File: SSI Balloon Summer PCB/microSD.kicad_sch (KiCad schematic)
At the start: 5 parts, among them J6 1040310811

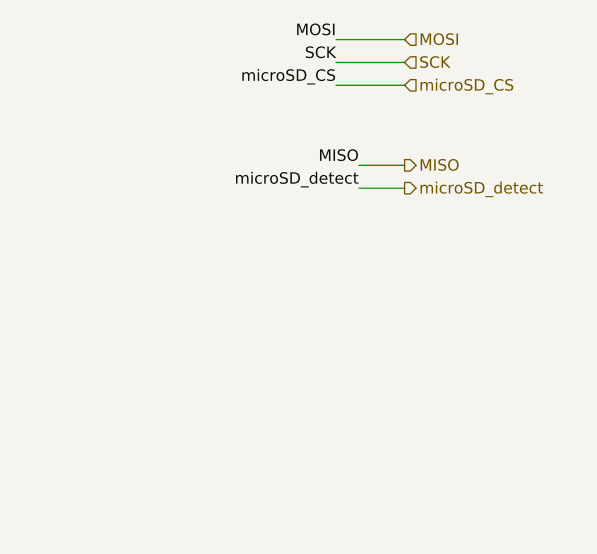
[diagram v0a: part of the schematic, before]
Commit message: Finished sensors + tidied up schematic
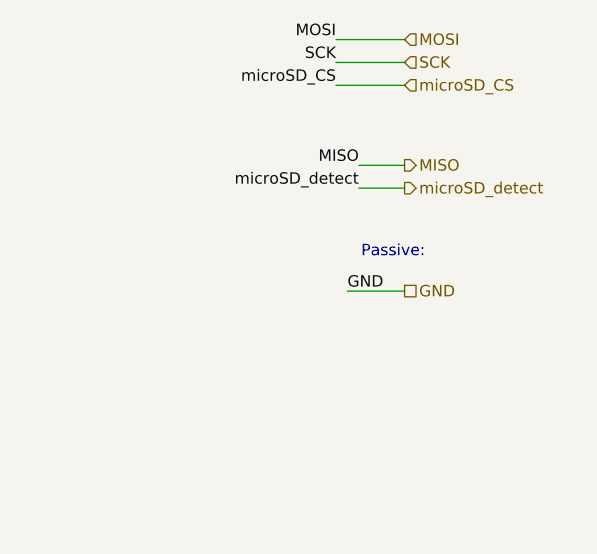
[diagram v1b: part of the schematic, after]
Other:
- note added: "Passive:"
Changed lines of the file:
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@@
 	(generator_version "10.0")
 	(paper "A4")
+	(text "Passive:"
+		(exclude_from_sim no)
+		(at 246.38 52.832 0)
+		(effects
+			(font
+				(size 1.27 1.27)
+			)
+		)
+	)
 	(text "microSD_detect: \nhigh if SD card detected\nlow if no SD card"
 		(exclude_from_sim no)
@@
 	(wire
 		(pts
+			(xy 241.3 57.15) (xy 247.65 57.15)
+		)
+		(stroke
+			(width 0)
+			(type default)
+		)
+	)
+	(wire
+		(pts
 			(xy 66.04 78.74) (xy 69.85 78.74)
 		)
@@
 		)
 	)
+	(label "GND"
+		(at 241.3 57.15 0)
+		(effects
+			(font
+				(size 1.27 1.27)
+			)
+			(justify left bottom)
+		)
+	)
 	(label "microSD_detect"
 		(at 144.78 78.74 180)
@@
 		)
 	)
+	(hierarchical_label "GND"
+		(shape passive)
+		(at 247.65 57.15 0)
+		(effects
+			(font
+				(size 1.27 1.27)
+			)
+			(justify left)
+		)
+	)

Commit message: Fixed I2C and SPI issues
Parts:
- added R26: 10k, symbol Device:R
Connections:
- net +3V3: now also R26.2
- net microSD_CS: now also R26.1
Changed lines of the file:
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@@
+	)
+	(junction
+		(at 62.23 78.74)
+		(diameter 0)
+		(color 0 0 0 0)
 	)
 	(junction
@@
 	(wire
 		(pts
+			(xy 62.23 76.2) (xy 62.23 78.74)
+		)
+		(stroke
+			(width 0)
+			(type default)
+		)
+	)
+	(wire
+		(pts
 			(xy 241.3 57.15) (xy 247.65 57.15)
 		)
@@
 	(wire
 		(pts
-			(xy 66.04 78.74) (xy 69.85 78.74)
+			(xy 57.15 78.74) (xy 62.23 78.74)
+		)
+		(stroke
+			(width 0)
+			(type default)
+		)
+	)
+	(wire
+		(pts
+			(xy 62.23 66.04) (xy 62.23 68.58)
 		)
 		(stroke
@@
 		(pts
 			(xy 240.03 29.21) (xy 247.65 29.21)
+		)
+		(stroke
+			(width 0)
+			(type default)
+		)
+	)
+	(wire
+		(pts
+			(xy 62.23 78.74) (xy 69.85 78.74)
 		)
 		(stroke
@@
 	)
 	(label "microSD_CS"
-		(at 66.04 78.74 180)
+		(at 57.15 78.74 180)
 		(effects
 			(font
@@
 			)
 			(justify right bottom)
+		)
+	)
+	(label "+3V3"
+		(at 62.23 66.04 0)
+		(effects
+			(font
+				(size 1.27 1.27)
+			)
+			(justify left bottom)
 		)
 	)
@@
 					(unit 1)
 				)
+			)
+		)
+	)
+	(symbol
+		(lib_id "Device:R")
+		(at 62.23 72.39 180)
+		(unit 1)
+		(body_style 1)
+		(exclude_from_sim no)
+		(in_bom yes)
+		(on_board yes)
+		(in_pos_files yes)
+		(dnp no)
+		(property "Reference" "R26"
+			(at 60.198 73.66 0)
+			(show_name no)
+			(do_not_autoplace no)
+			(effects
+				(font
+					(size 1.27 1.27)
+				)
+				(justify left)
+			)
+		)
+		(property "Value" "10k"
+			(at 60.198 71.12 0)
+			(show_name no)
+			(do_not_autoplace no)
+			(effects
+				(font
+					(size 1.27 1.27)
+				)
+				(justify left)
+			)
+		)
+		(property "Footprint" ""
+			(at 64.008 72.39 90)
+			(hide yes)
+			(show_name no)
+			(do_not_autoplace no)
+			(effects
+				(font
+					(size 1.27 1.27)
+				)
+			)
+		)
+		(property "Datasheet" ""
+			(at 62.23 72.39 0)
+			(hide yes)
+			(show_name no)
+			(do_not_autoplace no)
+			(effects
+				(font
+					(size 1.27 1.27)
+				)
+			)
+		)
+		(property "Description" "Resistor"
+			(at 62.23 72.39 0)
+			(hide yes)
+			(show_name no)
+			(do_not_autoplace no)
+			(effects
+				(font
+					(size 1.27 1.27)
+				)
+			)
+		)
+		(pin "1"
+		)
+		(pin "2"
+		)
+		(instances
+			(project "SSI Summer Balloons"
+				(path "/3c45a535-6e6b-4825-ad52-82c10cbe7866/0df234a1-8d04-4ff9-99d5-3634fc842029"
+					(reference "R26")
+					(unit 1)
+				)

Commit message: Fixed ERC - no ERC errors
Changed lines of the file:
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@@
+	(wire
+		(pts
+			(xy 41.91 81.28) (xy 41.91 83.82)
+		)
+		(stroke
+			(width 0)
+			(type default)
+		)
+	)
+	(wire
+		(pts
+			(xy 125.73 78.74) (xy 144.78 78.74)
+		)
+		(stroke
+			(width 0)
+			(type default)
+		)
+	)
+	(wire
+		(pts
+			(xy 66.04 86.36) (xy 69.85 86.36)
+		)
+		(stroke
+			(width 0)
+			(type default)
+		)
+	)
+	(wire
+		(pts
+			(xy 130.81 83.82) (xy 125.73 83.82)
+		)
+		(stroke
+			(width 0)
+			(type default)
+		)
+	)
+	(wire
+		(pts
+			(xy 194.31 119.38) (xy 194.31 121.92)
+		)
+		(stroke
+			(width 0)
+			(type default)
+		)
+	)
+	(wire
+		(pts
+			(xy 242.57 45.72) (xy 247.65 45.72)
+		)
+		(stroke
+			(width 0)
+			(type default)
+		)
+	)
+	(wire
+		(pts
+			(xy 240.03 34.29) (xy 247.65 34.29)
+		)
+		(stroke
+			(width 0)
+			(type default)
+		)
+	)
+	(wire
+		(pts
+			(xy 240.03 29.21) (xy 247.65 29.21)
+		)
+		(stroke
+			(width 0)
+			(type default)
+		)
+	)
 	(wire
 		(pts
@@
 	(wire
 		(pts
-			(xy 125.73 78.74) (xy 144.78 78.74)
+			(xy 62.23 78.74) (xy 69.85 78.74)
 		)
 		(stroke
@@
 	(wire
 		(pts
-			(xy 66.04 86.36) (xy 69.85 86.36)
+			(xy 240.03 31.75) (xy 247.65 31.75)
 		)
 		(stroke
@@
 	(wire
 		(pts
-			(xy 130.81 83.82) (xy 125.73 83.82)
+			(xy 194.31 100.33) (xy 194.31 104.14)
 		)
 		(stroke
@@
 		)
 	)
-	(wire
-		(pts
-			(xy 194.31 119.38) (xy 194.31 121.92)
-		)
-		(stroke
-			(width 0)
-			(type default)
-		)
-	)
-	(wire
-		(pts
-			(xy 242.57 45.72) (xy 247.65 45.72)
-		)
-		(stroke
-			(width 0)
-			(type default)
-		)
-	)
-	(wire
-		(pts
-			(xy 240.03 34.29) (xy 247.65 34.29)
-		)
-		(stroke
-			(width 0)
-			(type default)
-		)
-	)
-	(wire
-		(pts
-			(xy 240.03 29.21) (xy 247.65 29.21)
-		)
-		(stroke
-			(width 0)
-			(type default)
-		)
-	)
-	(wire
-		(pts
-			(xy 62.23 78.74) (xy 69.85 78.74)
-		)
-		(stroke
-			(width 0)
-			(type default)
-		)
-	)
-	(wire
-		(pts
-			(xy 240.03 31.75) (xy 247.65 31.75)
-		)
-		(stroke
-			(width 0)
-			(type default)
-		)
-	)
-	(wire
-		(pts
-			(xy 194.31 100.33) (xy 194.31 104.14)
-		)
-		(stroke
-			(width 0)
-			(type default)
-		)
-	)
 	(label "microSD_detect"
 		(at 194.31 100.33 0)
@@
 			)
 			(justify right bottom)
+		)
+	)
+	(label "+3V3"
+		(at 41.91 81.28 0)
+		(effects
+			(font
+				(size 1.27 1.27)
+			)
+			(justify left bottom)
 		)
 	)
@@
 					(unit 1)
 				)
-			)
-		)
-	)
-	(symbol
-		(lib_id "power:+3V3")
-		(at 41.91 83.82 0)
-		(unit 1)
-		(body_style 1)
-		(exclude_from_sim no)
-		(in_bom yes)
-		(on_board yes)
-		(in_pos_files yes)
-		(dnp no)
-		(fields_autoplaced yes)
-		(property "Reference" "#PWR075"
-			(at 41.91 87.63 0)
-			(hide yes)
-			(show_name no)
-			(do_not_autoplace no)
-			(effects
-				(font
-					(size 1.27 1.27)
-				)
-			)
-		)
-		(property "Value" "+3V3"
-			(at 41.91 78.74 0)
-			(show_name no)
-			(do_not_autoplace no)
-			(effects
-				(font
-					(size 1.27 1.27)
-				)
-			)
-		)
-		(property "Footprint" ""
-			(at 41.91 83.82 0)
-			(hide yes)
-			(show_name no)
-			(do_not_autoplace no)
-			(effects
-				(font
-					(size 1.27 1.27)
-				)
-			)
-		)
-		(property "Datasheet" ""
-			(at 41.91 83.82 0)
-			(hide yes)
-			(show_name no)
-			(do_not_autoplace no)
-			(effects
-				(font
-					(size 1.27 1.27)
-				)
-			)
-		)
-		(property "Description" "Power symbol creates a global label with name \"+3V3\""
-			(at 41.91 83.82 0)
-			(hide yes)
-			(show_name no)
-			(do_not_autoplace no)
-			(effects
-				(font
-					(size 1.27 1.27)
-				)
-			)
-		)
-		(pin "1"
-		)
-		(instances
-			(project "SSI Summer Balloons"
-				(path "/3c45a535-6e6b-4825-ad52-82c10cbe7866/0df234a1-8d04-4ff9-99d5-3634fc842029"
-					(reference "#PWR075")
-					(unit 1)
-				)

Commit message: Layout placement for every sheet except PWR and SD card
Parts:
- C34: footprint (none) -> Capacitor_SMD:C_0603_1608Metric
- D1: footprint (none) -> LED_SMD:LED_0805_2012Metric
- R16, R17, R26: footprint (none) -> Resistor_SMD:R_0603_1608Metric
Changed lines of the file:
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@@
 			)
 		)
-		(property "Footprint" ""
+		(property "Footprint" "LED_SMD:LED_0805_2012Metric"
 			(at 194.31 115.57 0)
 			(hide yes)
@@
 			)
 		)
-		(property "Footprint" ""
+		(property "Footprint" "Resistor_SMD:R_0603_1608Metric"
 			(at 64.008 72.39 90)
 			(hide yes)
@@
 			)
 		)
-		(property "Footprint" ""
+		(property "Footprint" "Resistor_SMD:R_0603_1608Metric"
 			(at 143.002 82.55 90)
 			(hide yes)
@@
 			)
 		)
-		(property "Footprint" ""
+		(property "Footprint" "Capacitor_SMD:C_0603_1608Metric"
 			(at 42.8752 91.44 0)
 			(hide yes)
@@
 			)
 		)
-		(property "Footprint" ""
+		(property "Footprint" "Resistor_SMD:R_0603_1608Metric"
 			(at 192.532 107.95 90)
 			(hide yes)

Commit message: Reviewed sensor sheet
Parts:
- removed R16: 10k, Resistor_SMD:R_0603_1608Metric, symbol Device:R
- C34: footprint Capacitor_SMD:C_0603_1608Metric -> (none)
- D1: footprint LED_SMD:LED_0805_2012Metric -> (none)
- R17, R26: footprint Resistor_SMD:R_0603_1608Metric -> (none)
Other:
- moved on the sheet: D1, R17
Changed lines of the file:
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@@
 	(text "Indicator LED for SD card detection"
 		(exclude_from_sim no)
-		(at 227.076 110.49 0)
+		(at 177.546 88.9 0)
 		(effects
 			(font
@@
 	(wire
 		(pts
-			(xy 194.31 119.38) (xy 194.31 121.92)
+			(xy 144.78 97.79) (xy 144.78 100.33)
 		)
 		(stroke
@@
 	(wire
 		(pts
-			(xy 194.31 100.33) (xy 194.31 104.14)
-		)
-		(stroke
-			(width 0)
-			(type default)
-		)
-	)
-	(label "microSD_detect"
-		(at 194.31 100.33 0)
-		(effects
-			(font
-				(size 1.27 1.27)
-			)
-			(justify left bottom)
+			(xy 144.78 78.74) (xy 144.78 82.55)
+		)
+		(stroke
+			(width 0)
+			(type default)
 		)
 	)
@@
 	(symbol
 		(lib_id "Device:LED")
-		(at 194.31 115.57 90)
+		(at 144.78 93.98 90)
 		(unit 1)
 		(body_style 1)
@@
 		(fields_autoplaced yes)
 		(property "Reference" "D1"
-			(at 198.12 115.8874 90)
+			(at 148.59 94.2974 90)
 			(show_name no)
 			(do_not_autoplace no)
@@
 		)
 		(property "Value" "LED"
-			(at 198.12 118.4274 90)
+			(at 148.59 96.8374 90)
 			(show_name no)
 			(do_not_autoplace no)
@@
 			)
 		)
-		(property "Footprint" "LED_SMD:LED_0805_2012Metric"
-			(at 194.31 115.57 0)
+		(property "Footprint" ""
+			(at 144.78 93.98 0)
 			(hide yes)
 			(show_name no)
@@
 		)
 		(property "Datasheet" ""
-			(at 194.31 115.57 0)
+			(at 144.78 93.98 0)
 			(hide yes)
 			(show_name no)
@@
 		)
 		(property "Description" "Light emitting diode"
-			(at 194.31 115.57 0)
+			(at 144.78 93.98 0)
 			(hide yes)
 			(show_name no)
@@
 		)
 		(property "Sim.Pins" "1=K 2=A"
-			(at 194.31 115.57 0)
+			(at 144.78 93.98 0)
 			(hide yes)
 			(show_name no)
@@
 			)
 		)
-		(property "Footprint" "Resistor_SMD:R_0603_1608Metric"
+		(property "Footprint" ""
 			(at 64.008 72.39 90)
 			(hide yes)
@@
 	(symbol
 		(lib_id "power:GND")
-		(at 194.31 121.92 0)
+		(at 144.78 100.33 0)
 		(unit 1)
 		(body_style 1)
@@
 		(fields_autoplaced yes)
 		(property "Reference" "#PWR080"
-			(at 194.31 128.27 0)
+			(at 144.78 106.68 0)
 			(hide yes)
 			(show_name no)
@@
 		)
 		(property "Value" "GND"
-			(at 194.31 127 0)
+			(at 144.78 105.41 0)
 			(show_name no)
 			(do_not_autoplace no)
@@
 		)
 		(property "Footprint" ""
-			(at 194.31 121.92 0)
+			(at 144.78 100.33 0)
 			(hide yes)
 			(show_name no)
@@
 		)
 		(property "Datasheet" ""
-			(at 194.31 121.92 0)
+			(at 144.78 100.33 0)
 			(hide yes)
 			(show_name no)
@@
 		)
 		(property "Description" "Power symbol creates a global label with name \"GND\" , ground"
-			(at 194.31 121.92 0)
+			(at 144.78 100.33 0)
 			(hide yes)
 			(show_name no)
@@
 	)
 	(symbol
-		(lib_id "Device:R")
-		(at 144.78 82.55 0)
-		(unit 1)
-		(body_style 1)
-		(exclude_from_sim no)
-		(in_bom yes)
-		(on_board yes)
-		(in_pos_files yes)
-		(dnp no)
-		(fields_autoplaced yes)
-		(property "Reference" "R16"
-			(at 147.32 81.2799 0)
-			(show_name no)
-			(do_not_autoplace no)
-			(effects
-				(font
-					(size 1.27 1.27)
-				)
-				(justify left)
-			)
-		)
-		(property "Value" "10k"
-			(at 147.32 83.8199 0)
-			(show_name no)
-			(do_not_autoplace no)
-			(effects
-				(font
-					(size 1.27 1.27)
-				)
-				(justify left)
-			)
-		)
-		(property "Footprint" "Resistor_SMD:R_0603_1608Metric"
-			(at 143.002 82.55 90)
-			(hide yes)
-			(show_name no)
-			(do_not_autoplace no)
-			(effects
-				(font
-					(size 1.27 1.27)
-				)
-			)
-		)
-		(property "Datasheet" ""
-			(at 144.78 82.55 0)
-			(hide yes)
-			(show_name no)
-			(do_not_autoplace no)
-			(effects
-				(font
-					(size 1.27 1.27)
-				)
-			)
-		)
-		(property "Description" "Resistor"
-			(at 144.78 82.55 0)
-			(hide yes)
-			(show_name no)
-			(do_not_autoplace no)
-			(effects
-				(font
-					(size 1.27 1.27)
-				)
-			)
-		)
-		(pin "1"
-		)
-		(pin "2"
-		)
-		(instances
-			(project "SSI Summer Balloons"
-				(path "/3c45a535-6e6b-4825-ad52-82c10cbe7866/0df234a1-8d04-4ff9-99d5-3634fc842029"
-					(reference "R16")
-					(unit 1)
-				)
-			)
-		)
-	)
-	(symbol
 		(lib_id "power:GND")
 		(at 41.91 91.44 0)
@@
 			)
 		)
-		(property "Footprint" "Capacitor_SMD:C_0603_1608Metric"
+		(property "Footprint" ""
 			(at 42.8752 91.44 0)
 			(hide yes)
@@
 	)
 	(symbol
-		(lib_id "power:GND")
+		(lib_id "Device:R")
 		(at 144.78 86.36 0)
 		(unit 1)
@@
 		(dnp no)
 		(fields_autoplaced yes)
-		(property "Reference" "#PWR078"
-			(at 144.78 92.71 0)
-			(hide yes)
-			(show_name no)
-			(do_not_autoplace no)
-			(effects
-				(font
-					(size 1.27 1.27)
-				)
-			)
-		)
-		(property "Value" "GND"
-			(at 144.78 91.44 0)
-			(show_name no)
-			(do_not_autoplace no)
-			(effects
-				(font
-					(size 1.27 1.27)
-				)
+		(property "Reference" "R17"
+			(at 147.32 85.0899 0)
+			(show_name no)
+			(do_not_autoplace no)
+			(effects
+				(font
+					(size 1.27 1.27)
+				)
+				(justify left)
+			)
+		)
+		(property "Value" "330R"
+			(at 147.32 87.6299 0)
+			(show_name no)
+			(do_not_autoplace no)
+			(effects
+				(font
+					(size 1.27 1.27)
+				)
+				(justify left)
 			)
 		)
 		(property "Footprint" ""
-			(at 144.78 86.36 0)
+			(at 143.002 86.36 90)
 			(hide yes)
 			(show_name no)
@@
 			)
 		)
-		(property "Description" "Power symbol creates a global label with name \"GND\" , ground"
+		(property "Description" "Resistor"
 			(at 144.78 86.36 0)
 			(hide yes)
 			(show_name no)
-			(do_not_autoplace no)
-			(effects
-				(font
-					(size 1.27 1.27)
-				)
-			)
-		)
-		(pin "1"
-		)
-		(instances
-			(project "SSI Summer Balloons"
-				(path "/3c45a535-6e6b-4825-ad52-82c10cbe7866/0df234a1-8d04-4ff9-99d5-3634fc842029"
-					(reference "#PWR078")
-					(unit 1)
-				)
-			)
-		)
-	)
-	(symbol
-		(lib_id "Device:R")
-		(at 194.31 107.95 0)
-		(unit 1)
-		(body_style 1)
-		(exclude_from_sim no)
-		(in_bom yes)
-		(on_board yes)
-		(in_pos_files yes)
-		(dnp no)
-		(fields_autoplaced yes)
-		(property "Reference" "R17"
-			(at 196.85 106.6799 0)
-			(show_name no)
-			(do_not_autoplace no)
-			(effects
-				(font
-					(size 1.27 1.27)
-				)
-				(justify left)
-			)
-		)
-		(property "Value" "330R"
-			(at 196.85 109.2199 0)
-			(show_name no)
-			(do_not_autoplace no)
-			(effects
-				(font
-					(size 1.27 1.27)
-				)
-				(justify left)
-			)
-		)
-		(property "Footprint" "Resistor_SMD:R_0603_1608Metric"
-			(at 192.532 107.95 90)
-			(hide yes)
-			(show_name no)
-			(do_not_autoplace no)
-			(effects
-				(font
-					(size 1.27 1.27)
-				)
-			)
-		)
-		(property "Datasheet" ""
-			(at 194.31 107.95 0)
-			(hide yes)
-			(show_name no)
-			(do_not_autoplace no)
-			(effects
-				(font
-					(size 1.27 1.27)
-				)
-			)
-		)
-		(property "Description" "Resistor"
-			(at 194.31 107.95 0)
-			(hide yes)
-			(show_name no)

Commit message: Overhauled power symbols for consistency and ERC
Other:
- note removed: "Passive:"
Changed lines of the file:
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@@
 	(generator_version "10.0")
 	(paper "A4")
-	(text "Passive:"
-		(exclude_from_sim no)
-		(at 246.38 52.832 0)
-		(effects
-			(font
-				(size 1.27 1.27)
-			)
-		)
-	)
 	(text "microSD_detect: \nhigh if SD card detected\nlow if no SD card"
 		(exclude_from_sim no)
@@
 	(wire
 		(pts
-			(xy 241.3 57.15) (xy 247.65 57.15)
-		)
-		(stroke
-			(width 0)
-			(type default)
-		)
-	)
-	(wire
-		(pts
 			(xy 57.15 78.74) (xy 62.23 78.74)
 		)
@@
 		)
 	)
-	(label "+3V3"
-		(at 41.91 81.28 0)
-		(effects
-			(font
-				(size 1.27 1.27)
-			)
-			(justify left bottom)
-		)
-	)
 	(label "SCK"
 		(at 66.04 86.36 180)
@@
 		)
 	)
-	(label "GND"
-		(at 241.3 57.15 0)
-		(effects
-			(font
-				(size 1.27 1.27)
-			)
-			(justify left bottom)
-		)
-	)
 	(label "microSD_detect"
 		(at 144.78 78.74 180)
@@
 			)
 			(justify right bottom)
-		)
-	)
-	(label "+3V3"
-		(at 62.23 66.04 0)
-		(effects
-			(font
-				(size 1.27 1.27)
-			)
-			(justify left bottom)
-		)
-	)
-	(hierarchical_label "GND"
-		(shape passive)
-		(at 247.65 57.15 0)
-		(effects
-			(font
-				(size 1.27 1.27)
-			)
-			(justify left)
 		)
 	)
@@
 	)
 	(symbol
+		(lib_id "power:+3V3")
+		(at 41.91 81.28 0)
+		(unit 1)
+		(body_style 1)
+		(exclude_from_sim no)
+		(in_bom yes)
+		(on_board yes)
+		(in_pos_files yes)
+		(dnp no)
+		(fields_autoplaced yes)
+		(property "Reference" "#PWR0109"
+			(at 41.91 85.09 0)
+			(hide yes)
+			(show_name no)
+			(do_not_autoplace no)
+			(effects
+				(font
+					(size 1.27 1.27)
+				)
+			)
+		)
+		(property "Value" "+3V3"
+			(at 41.91 76.2 0)
+			(show_name no)
+			(do_not_autoplace no)
+			(effects
+				(font
+					(size 1.27 1.27)
+				)
+			)
+		)
+		(property "Footprint" ""
+			(at 41.91 81.28 0)
+			(hide yes)
+			(show_name no)
+			(do_not_autoplace no)
+			(effects
+				(font
+					(size 1.27 1.27)
+				)
+			)
+		)
+		(property "Datasheet" ""
+			(at 41.91 81.28 0)
+			(hide yes)
+			(show_name no)
+			(do_not_autoplace no)
+			(effects
+				(font
+					(size 1.27 1.27)
+				)
+			)
+		)
+		(property "Description" "Power symbol creates a global label with name \"+3V3\""
+			(at 41.91 81.28 0)
+			(hide yes)
+			(show_name no)
+			(do_not_autoplace no)
+			(effects
+				(font
+					(size 1.27 1.27)
+				)
+			)
+		)
+		(pin "1"
+		)
+		(instances
+			(project "SSI Summer Balloons"
+				(path "/3c45a535-6e6b-4825-ad52-82c10cbe7866/0df234a1-8d04-4ff9-99d5-3634fc842029"
+					(reference "#PWR0109")
+					(unit 1)
+				)
+			)
+		)
+	)
+	(symbol
 		(lib_id "power:GND")
 		(at 125.73 86.36 0)
@@
 					(unit 1)
 				)
+			)
+		)
+	)
+	(symbol
+		(lib_id "power:+3V3")
+		(at 62.23 66.04 0)
+		(unit 1)
+		(body_style 1)
+		(exclude_from_sim no)
+		(in_bom yes)
+		(on_board yes)
+		(in_pos_files yes)
+		(dnp no)
+		(fields_autoplaced yes)
+		(property "Reference" "#PWR0108"
+			(at 62.23 69.85 0)
+			(hide yes)
+			(show_name no)
+			(do_not_autoplace no)
+			(effects
+				(font
+					(size 1.27 1.27)
+				)
+			)
+		)
+		(property "Value" "+3V3"
+			(at 62.23 60.96 0)
+			(show_name no)
+			(do_not_autoplace no)
+			(effects
+				(font
+					(size 1.27 1.27)
+				)
+			)
+		)
+		(property "Footprint" ""
+			(at 62.23 66.04 0)
+			(hide yes)
+			(show_name no)
+			(do_not_autoplace no)
+			(effects
+				(font
+					(size 1.27 1.27)
+				)
+			)
+		)
+		(property "Datasheet" ""
+			(at 62.23 66.04 0)
+			(hide yes)
+			(show_name no)
+			(do_not_autoplace no)
+			(effects
+				(font
+					(size 1.27 1.27)
+				)
+			)
+		)
+		(property "Description" "Power symbol creates a global label with name \"+3V3\""
+			(at 62.23 66.04 0)
+			(hide yes)
+			(show_name no)
+			(do_not_autoplace no)
+			(effects
+				(font
+					(size 1.27 1.27)
+				)
+			)
+		)
+		(pin "1"
+		)
+		(instances
+			(project "SSI Summer Balloons"
+				(path "/3c45a535-6e6b-4825-ad52-82c10cbe7866/0df234a1-8d04-4ff9-99d5-3634fc842029"
+					(reference "#PWR0108")
+					(unit 1)
+				)

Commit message: fixed footprints
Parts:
- C34: footprint (none) -> Capacitor_SMD:C_0603_1608Metric
- D1: footprint (none) -> LED_SMD:LED_0805_2012Metric
- R17, R26: footprint (none) -> Resistor_SMD:R_0603_1608Metric
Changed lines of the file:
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@@
 			)
 		)
-		(property "Footprint" ""
+		(property "Footprint" "LED_SMD:LED_0805_2012Metric"
 			(at 144.78 93.98 0)
 			(hide yes)
@@
 			)
 		)
-		(property "Footprint" ""
+		(property "Footprint" "Resistor_SMD:R_0603_1608Metric"
 			(at 64.008 72.39 90)
 			(hide yes)
@@
 			)
 		)
-		(property "Footprint" ""
+		(property "Footprint" "Capacitor_SMD:C_0603_1608Metric"
 			(at 42.8752 91.44 0)
 			(hide yes)
@@
 			)
 		)
-		(property "Footprint" ""
+		(property "Footprint" "Resistor_SMD:R_0603_1608Metric"
 			(at 143.002 86.36 90)
 			(hide yes)
